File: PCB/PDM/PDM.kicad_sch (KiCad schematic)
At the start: 10 parts, among them IC4 TS5A21366DCUR, Q1 MMBT3904, U1 STM32F405RGTx, U2 MCP2561-E-SN, U3 MCP2561-E-SN

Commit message: Added another high-side switch 2x7A + 2x4A SPI
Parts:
- removed U1: STM32F405RGTx, Package_QFP:LQFP-64_10x10mm_P0.5mm, symbol MCU_ST_STM32F4:STM32F405RGTx
- added IC5, IC6: TMP126NDCKR, PDM_Additional:SOT65P210X110-6N, symbol PDM_additional:TMP126NDCKR
- added R18, R19: 10k, Resistor_SMD:R_0402_1005Metric, symbol Device:R_Small
- C13: footprint (none) -> Capacitor_SMD:C_0805_2012Metric
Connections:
- net +3.3V: now also IC5.6 (VDD), IC6.6 (VDD), R18.1, R19.2
- net GND: now also IC5.2 (GND), IC6.2 (GND)
- new net SPI2_CLK: IC5.4 (SCLK), IC6.4 (SCLK)
- new net SPI2_IO: IC5.3 (SIO), IC6.3 (SIO)
- new net TEMP1_ALERT: IC5.5 (~{ALERT}), R18.2
- new net TEMP1_CS: IC5.1 (~{CS})
- new net TEMP2_ALERT: IC6.5 (~{ALERT}), R19.1
- new net TEMP2_CS: IC6.1 (~{CS})
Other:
- added sheet BTS50010-1TAE1 (BTS50010-1TAE.kicad_sch)
- added sheet BTS70021EPP2 (BTS70021EPP.kicad_sch)
- added sheet BTS70021EPP3 (BTS70021EPP.kicad_sch)
- added sheet BTS722204ESAXUMA1 (BTS722204ESAXUMA1.kicad_sch)
- added sheet BTS722204ESAXUMA2 (BTS722204ESAXUMA1.kicad_sch)
- added sheet MCU (mcu.kicad_sch)
- note added: "POWER MANAGMENT SECTION"
- note added: "Temperature sensors"
- moved on the sheet: BZ1, Q1, R11

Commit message: Added Reverse polarity protection
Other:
- added sheet lm5050_node (lm5050_node.kicad_sch)
- added sheet lm5050_node1 (lm5050_node.kicad_sch)
- note added: "Add TVS diodes for protection and output protection"
- note added: "High-Side switches"
- note added: "Reverse polarity protection using LM5050-MK1 - 2x REDUNDANT"

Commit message: Fuck christmas & low side section
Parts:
- added D10, D11, D9: WS2812B, LED_SMD:LED_WS2812B-2020_PLCC4_2.0x2.0mm, symbol LED:WS2812B
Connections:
- net +5V: now also D10.1 (VDD), D11.1 (VDD), D9.1 (VDD)
- net GND: now also D10.3 (VSS), D11.3 (VSS), D9.3 (VSS)
- new net: D10.4 (DIN), D9.2 (DOUT)
- new net: D10.2 (DOUT), D11.4 (DIN)
- new net STATUS_LED_D: D9.4 (DIN)
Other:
- added sheet TLE9104SH (TLE9104SH.kicad_sch)
- note added: "Low-Side switches"
- note added: "MCU"
- moved on the sheet: C13, IC4, R16, R17, U3

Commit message: Concept revision and MCU section changes
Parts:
- removed BZ1: Buzzer, symbol Device:Buzzer
- removed D10, D11, D9: WS2812B, LED_SMD:LED_WS2812B-2020_PLCC4_2.0x2.0mm, symbol LED:WS2812B
- removed Q1: MMBT3904, Package_TO_SOT_SMD:SOT-23, symbol Transistor_BJT:MMBT3904
- removed R11: 1k, Resistor_SMD:R_0402_1005Metric, symbol Device:R_Small
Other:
- removed sheet BTS70021EPP0
- added sheet VNF1048FTR (VNF1048FTR.kicad_sch)
- added sheet ocp_concept1 (ocp_concept1.kicad_sch)
- added sheet user_peripheral (user_peripheral.kicad_sch.kicad_sch)
- sheet MCU ports: added ADC1_IN[1..16], CAN1_RX, CAN1_TX, CAN2_RX, CAN2_TX, SPI1{SCK, MISO, MOSI}, SPI3{SCK, MISO, MOSI}; removed none

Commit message: MCU preliminary scheme and qspi flash
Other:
- removed sheet BTS50010-1TAE1
- removed sheet BTS70021EPP1
- removed sheet BTS70021EPP2
- removed sheet BTS70021EPP3
- removed sheet ocp_concept1
- sheet MCU ports: added I2C1_SCL, I2C1_SDA, NCS_SECA[1..6], SPI2{SCK, MISO, MOSI}, SWCLK, SWDIO, USB_OTG_FS_DM_OPT, USB_OTG_FS_DP_OPT; removed none
- note added: "Consider changing to SN65HVD234-Q1 for 3.3V and Q1 cert"

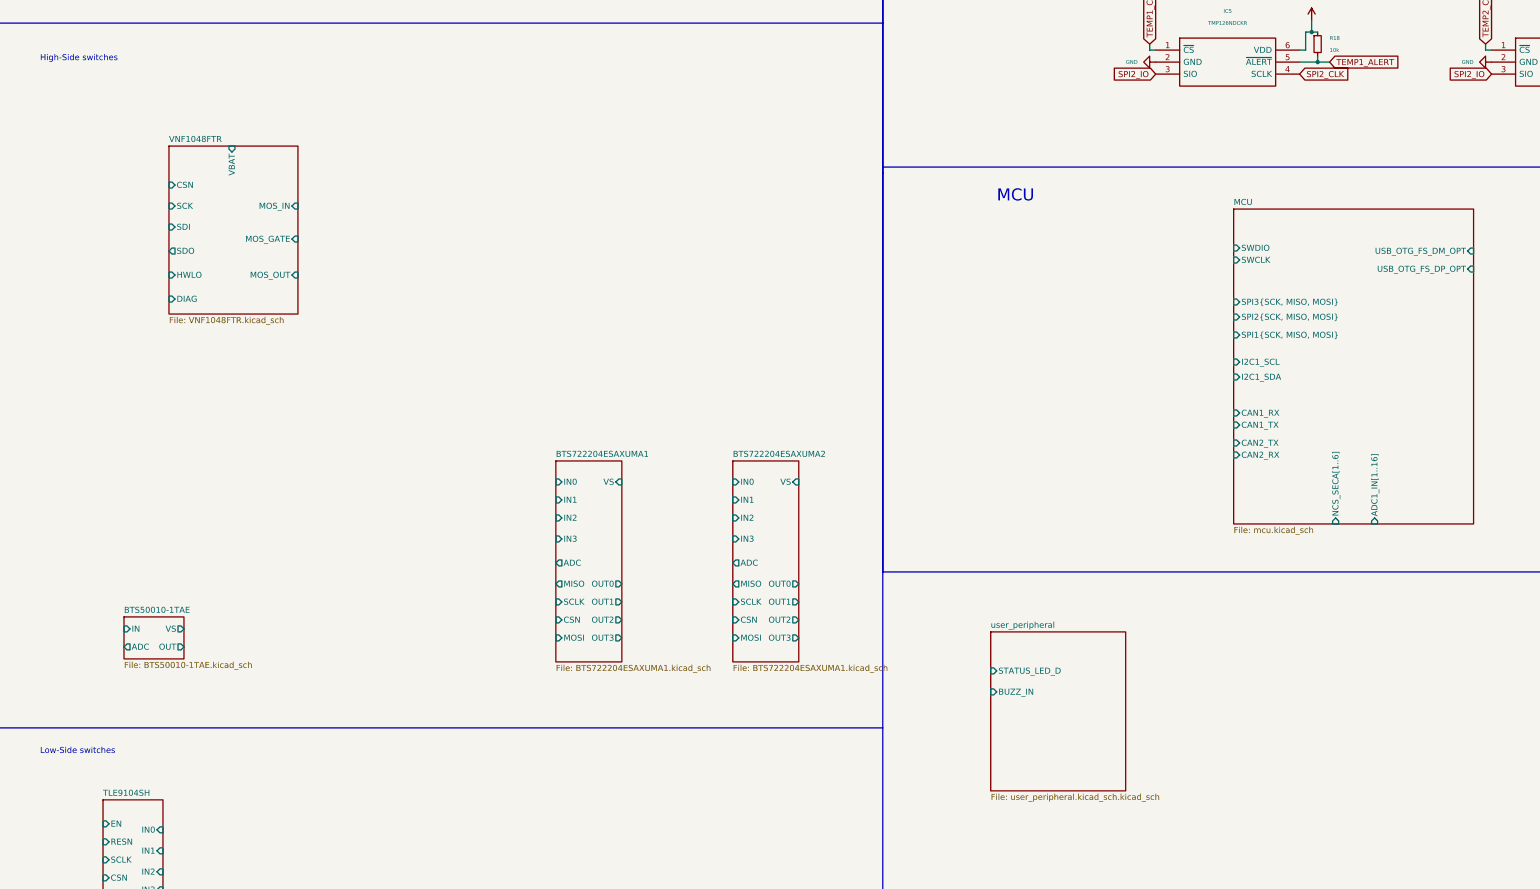
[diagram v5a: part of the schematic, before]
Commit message: Added new type of high side driver based on VNF1048 + STL135
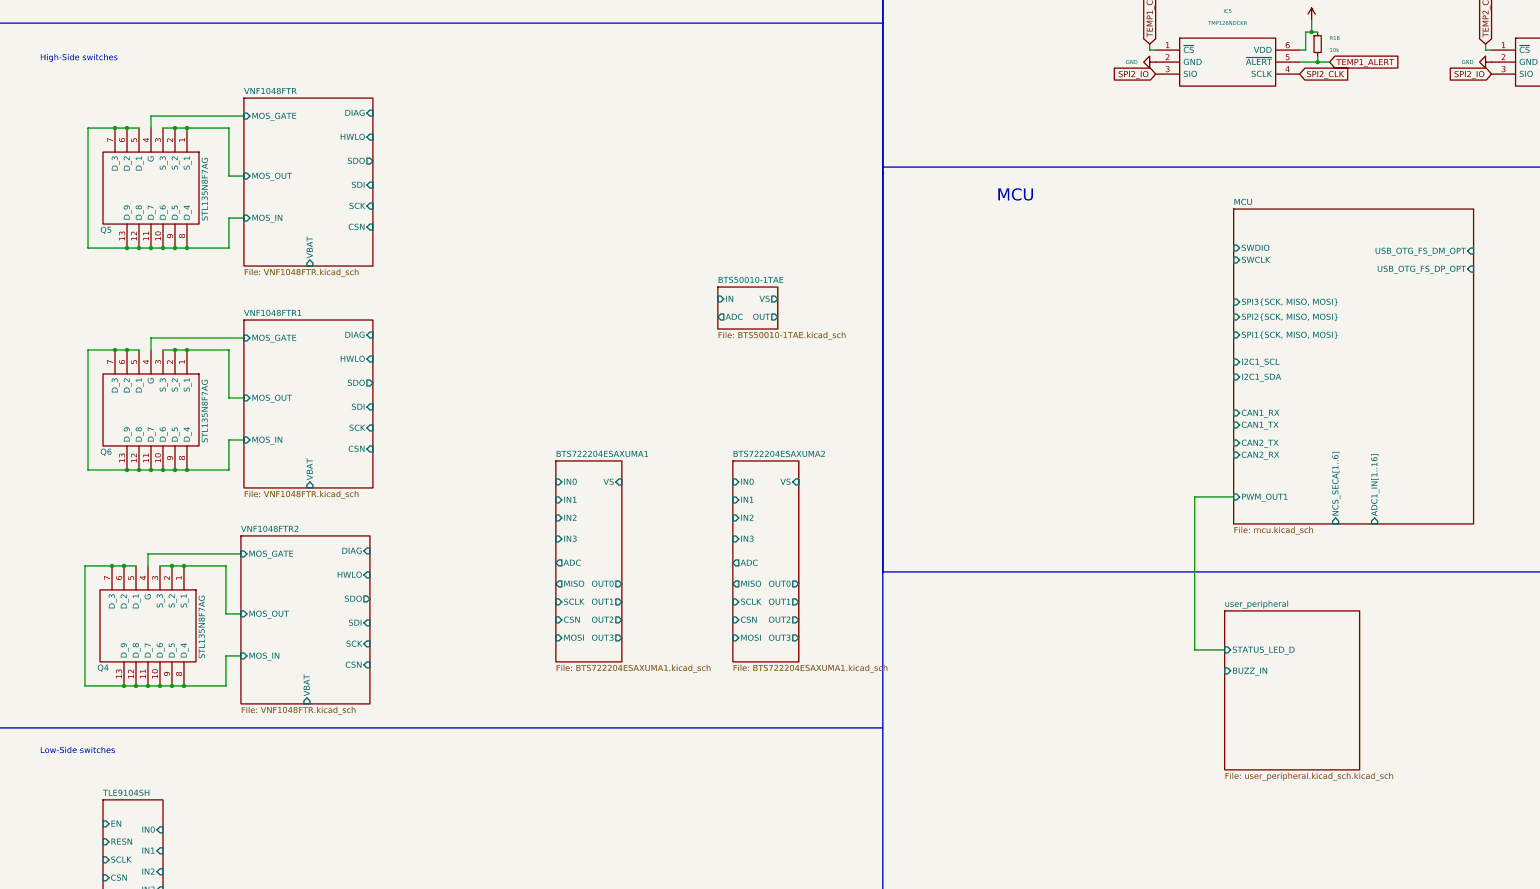
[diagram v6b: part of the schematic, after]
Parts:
- added Q4, Q5, Q6: STL135N8F7AG, STL135N8F7AG, symbol PDM_additional:STL135N8F7AG
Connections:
- net VNF1048FTR/MOS_GATE: now also Q5.4 (G)
- net VNF1048FTR/MOS_IN: now also Q5.10 (D_6), Q5.11 (D_7), Q5.12 (D_8), Q5.13 (D_9), Q5.5 (D_1), Q5.6 (D_2), Q5.7 (D_3), Q5.8 (D_4), Q5.9 (D_5)
- net VNF1048FTR/MOS_OUT: now also Q5.1 (S_1), Q5.2 (S_2), Q5.3 (S_3)
- new net VNF1048FTR1/MOS_GATE: Q6.4 (G)
- new net VNF1048FTR1/MOS_IN: Q6.10 (D_6), Q6.11 (D_7), Q6.12 (D_8), Q6.13 (D_9), Q6.5 (D_1), Q6.6 (D_2), Q6.7 (D_3), Q6.8 (D_4), Q6.9 (D_5)
- new net VNF1048FTR1/MOS_OUT: Q6.1 (S_1), Q6.2 (S_2), Q6.3 (S_3)
- new net VNF1048FTR2/MOS_GATE: Q4.4 (G)
- new net VNF1048FTR2/MOS_IN: Q4.10 (D_6), Q4.11 (D_7), Q4.12 (D_8), Q4.13 (D_9), Q4.5 (D_1), Q4.6 (D_2), Q4.7 (D_3), Q4.8 (D_4), Q4.9 (D_5)
- new net VNF1048FTR2/MOS_OUT: Q4.1 (S_1), Q4.2 (S_2), Q4.3 (S_3)
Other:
- added sheet VNF1048FTR1 (VNF1048FTR.kicad_sch)
- added sheet VNF1048FTR2 (VNF1048FTR.kicad_sch)
- sheet MCU ports: added PWM_OUT1; removed none

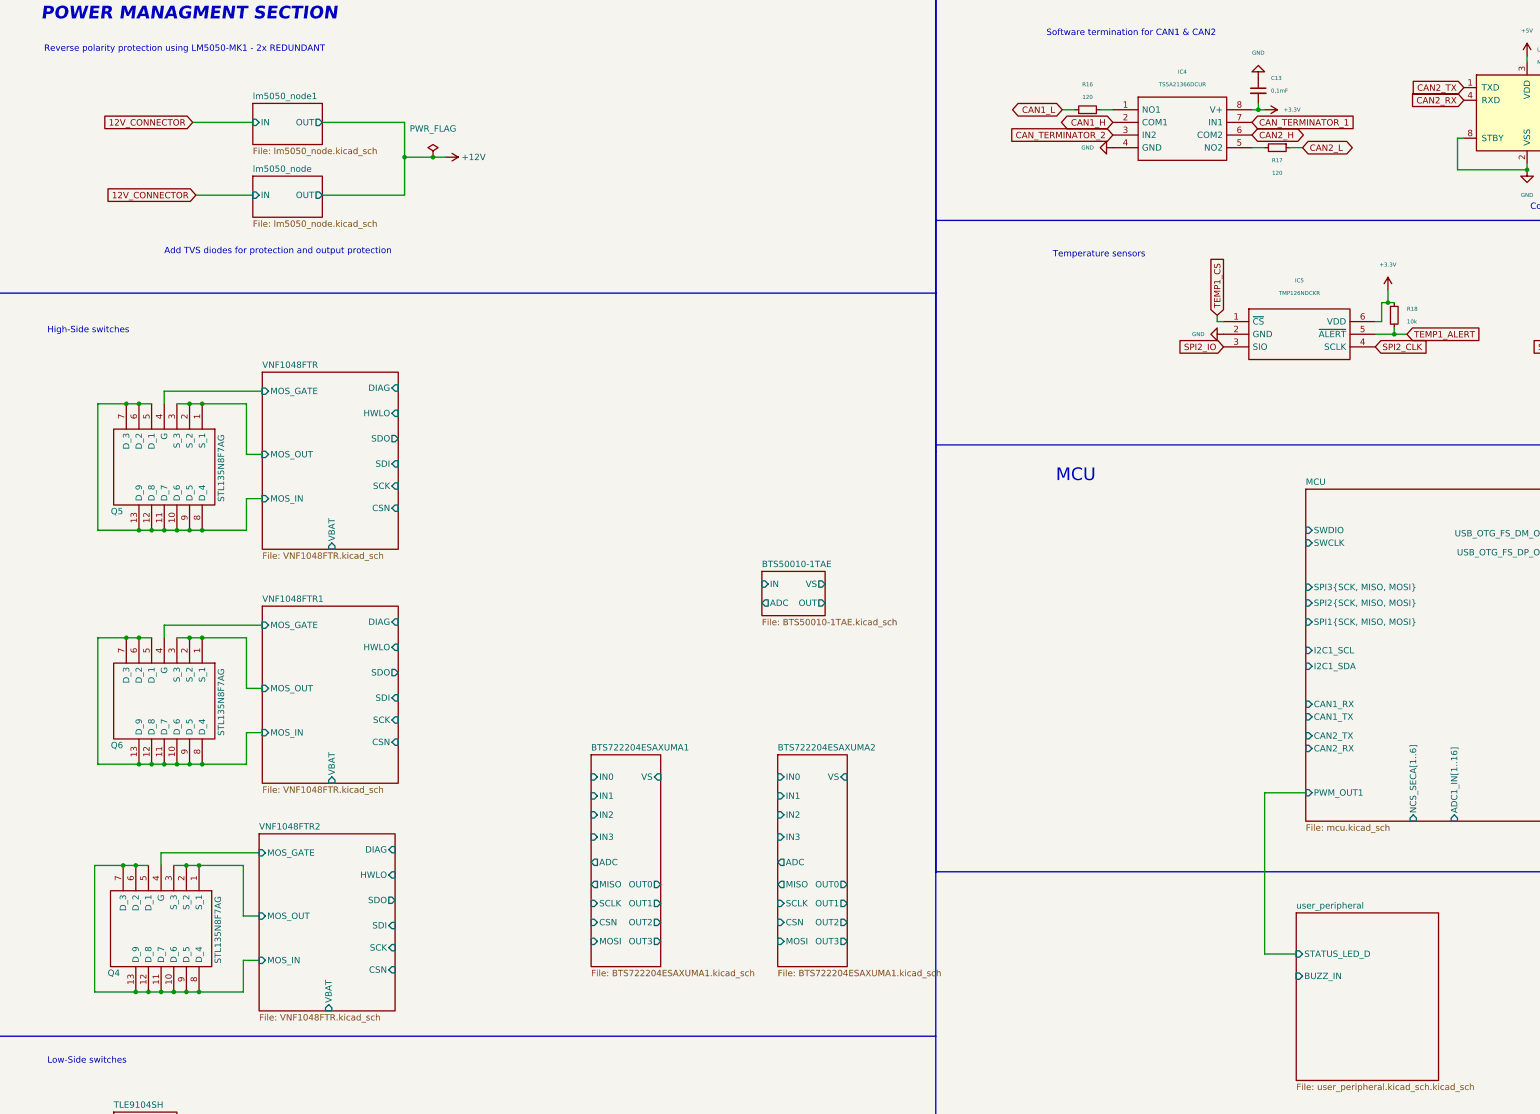
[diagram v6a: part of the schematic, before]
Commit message: Finished high side section & fixed some ERC's errors
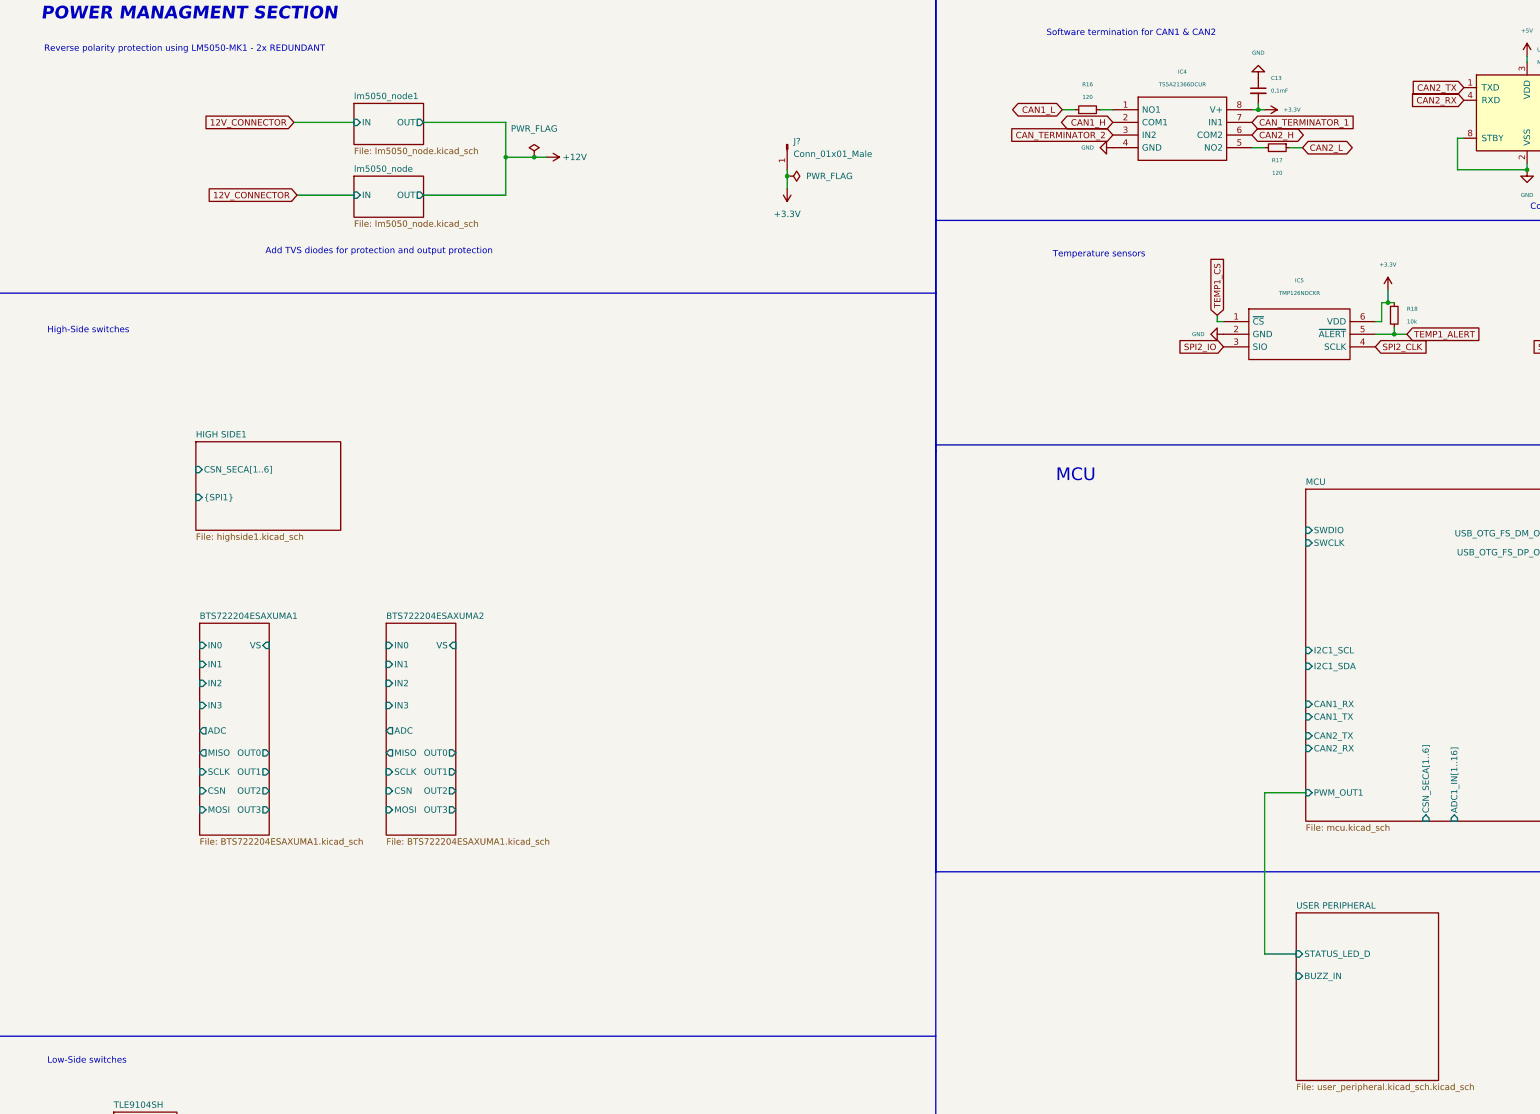
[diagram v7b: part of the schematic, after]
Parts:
- removed Q4, Q5, Q6: STL135N8F7AG, STL135N8F7AG, symbol PDM_additional:STL135N8F7AG
- added J?: Conn_01x01_Male, symbol Connector:Conn_01x01_Male
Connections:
- net +3.3V: now also J?.1 (Pin_1)
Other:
- sheet user_peripheral renamed USER PERIPHERAL
- removed sheet BTS50010-1TAE
- removed sheet VNF1048FTR
- removed sheet VNF1048FTR1
- removed sheet VNF1048FTR2
- added sheet HIGH SIDE1 (highside1.kicad_sch)
- sheet MCU ports: added CSN_SECA[1..6]; removed NCS_SECA[1..6], SPI1{SCK, MISO, MOSI}, SPI2{SCK, MISO, MOSI}, SPI3{SCK, MISO, MOSI}

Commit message: Minor changes in HS sechmatics
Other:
- sheet HIGH SIDE1 ports: added CSN[1..8]; removed CSN_SECA[1..6]
- sheet USER PERIPHERAL: file user_peripheral.kicad_sch.kicad_sch -> USER_PERIPHERAL.kicad_sch
